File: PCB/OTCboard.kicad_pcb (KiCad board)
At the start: 4 copper layers, 0 parts

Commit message: cramming for portfolio
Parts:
- added C1: C, Capacitor_SMD:C_0603_1608Metric_Pad1.08x0.95mm_HandSolder, F.Cu at (90.7, 80.7)
- added C2: C, Capacitor_SMD:C_0603_1608Metric_Pad1.08x0.95mm_HandSolder, F.Cu at (90.7, 83.2)
- added C3: 0.1uF, Capacitor_SMD:C_0603_1608Metric_Pad1.08x0.95mm_HandSolder, F.Cu at (90.7, 85.7)
- added C4: 10u, Capacitor_SMD:C_0805_2012Metric_Pad1.18x1.45mm_HandSolder, F.Cu at (93.8, 68.9)
- added C5: 1u, Capacitor_SMD:C_0805_2012Metric_Pad1.18x1.45mm_HandSolder, F.Cu at (93.8, 71.9)
- added C6: 1u, Capacitor_SMD:C_0805_2012Metric_Pad1.18x1.45mm_HandSolder, F.Cu at (93.8, 74.9)
- added D1: 1N5819HW-7-F, Diode_SMD:D_SOD-123, F.Cu at (91.8, 64.3)
- added D2: SP0503BAHT, Package_TO_SOT_SMD:SOT-143, F.Cu at (95.4, 59.8)
- added D3: PWR, LED_SMD:LED_0603_1608Metric_Pad1.05x0.95mm_HandSolder, F.Cu at (91.1, 58.7)
- added D4: PWR, LED_SMD:LED_0603_1608Metric_Pad1.05x0.95mm_HandSolder, F.Cu at (91.1, 61.3)
- added D5: SK6812MINI, LED_SMD:LED_SK6812MINI_PLCC4_3.5x3.5mm_P1.75mm, F.Cu at (71.8, 60.0)
- added D6: SK6812MINI, LED_SMD:LED_SK6812MINI_PLCC4_3.5x3.5mm_P1.75mm, F.Cu at (71.8, 65.1)
- added D7: SK6812MINI, LED_SMD:LED_SK6812MINI_PLCC4_3.5x3.5mm_P1.75mm, F.Cu at (71.8, 70.2)
- added J1: USB_C_Receptacle_USB2.0_16P, Connector_USB:USB_C_Receptacle_GCT_USB4105-xx-A_16P_TopMnt_Horizontal, F.Cu at (132.1, 53.7)
- added J2: Display, Connector_PinHeader_2.54mm:PinHeader_1x08_P2.54mm_Vertical, F.Cu at (66.2, 59.7)
- added R1: 10k, Resistor_SMD:R_0603_1608Metric_Pad0.98x0.95mm_HandSolder, F.Cu at (90.7, 88.2)
- added R2: 5.1k, Resistor_SMD:R_0603_1608Metric_Pad0.98x0.95mm_HandSolder, F.Cu at (89.2, 68.6)
- added R3: 5.1k, Resistor_SMD:R_0603_1608Metric_Pad0.98x0.95mm_HandSolder, F.Cu at (89.2, 71.2)
- added R4: 450, Resistor_SMD:R_0603_1608Metric_Pad0.98x0.95mm_HandSolder, F.Cu at (89.2, 73.7)
- added R5: 120, Resistor_SMD:R_0603_1608Metric_Pad0.98x0.95mm_HandSolder, F.Cu at (89.2, 76.2)
- added U1: STM32G491CETx, Package_QFP:LQFP-48_7x7mm_P0.5mm, F.Cu at (82.9, 85.1)
- added U2: TLV1117-33, Package_TO_SOT_SMD:SOT-223, F.Cu at (82.1, 71.6)
- added U3: DRV5055A3xDBZxQ1, Package_TO_SOT_SMD:SOT-23, F.Cu at (66.4, 84.0)
- added U4: DRV5055A3xDBZxQ1, Package_TO_SOT_SMD:SOT-23, F.Cu at (66.4, 88.4)
- added U5: DRV5055A3xDBZxQ1, Package_TO_SOT_SMD:SOT-23, F.Cu at (66.4, 92.9)
- added Y1: Crystal, Crystal:Crystal_SMD_Abracon_ABM3-2Pin_5.0x3.2mm, F.Cu at (81.0, 93.4)

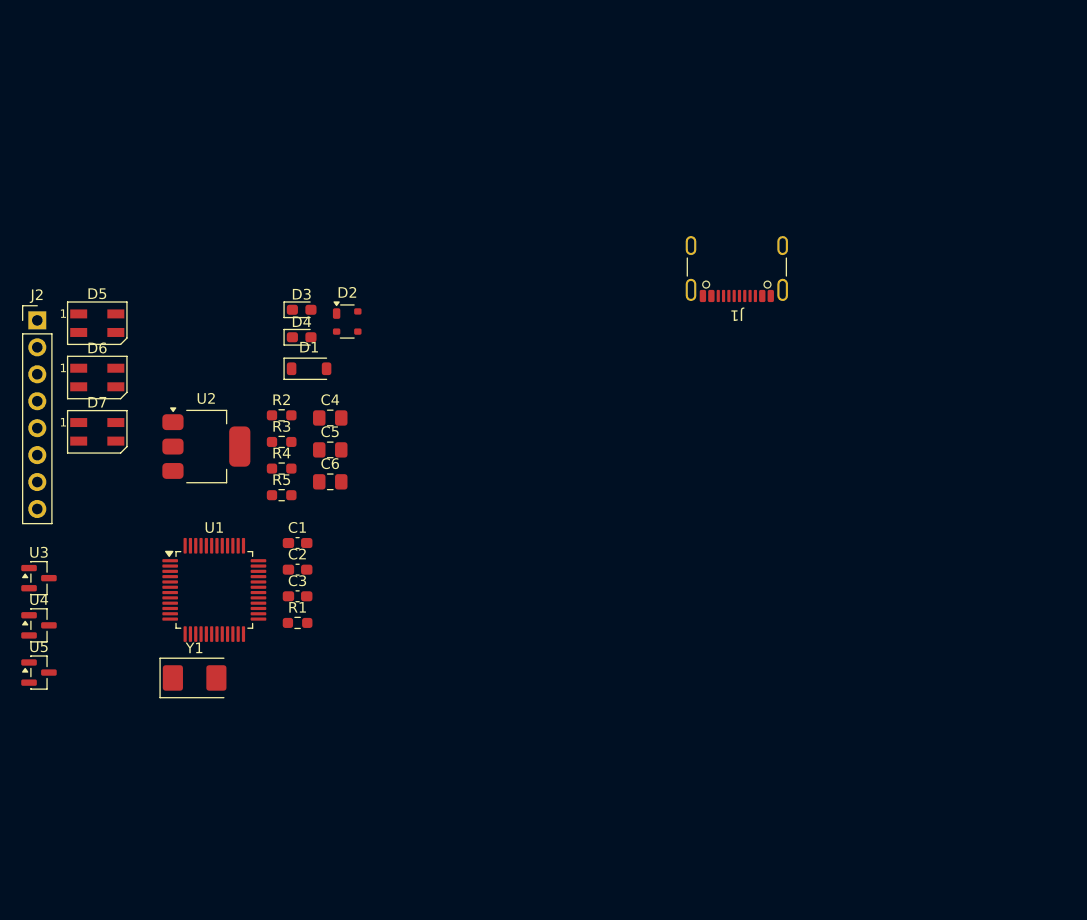
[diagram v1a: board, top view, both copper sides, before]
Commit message: only need to find boot and reset footprints
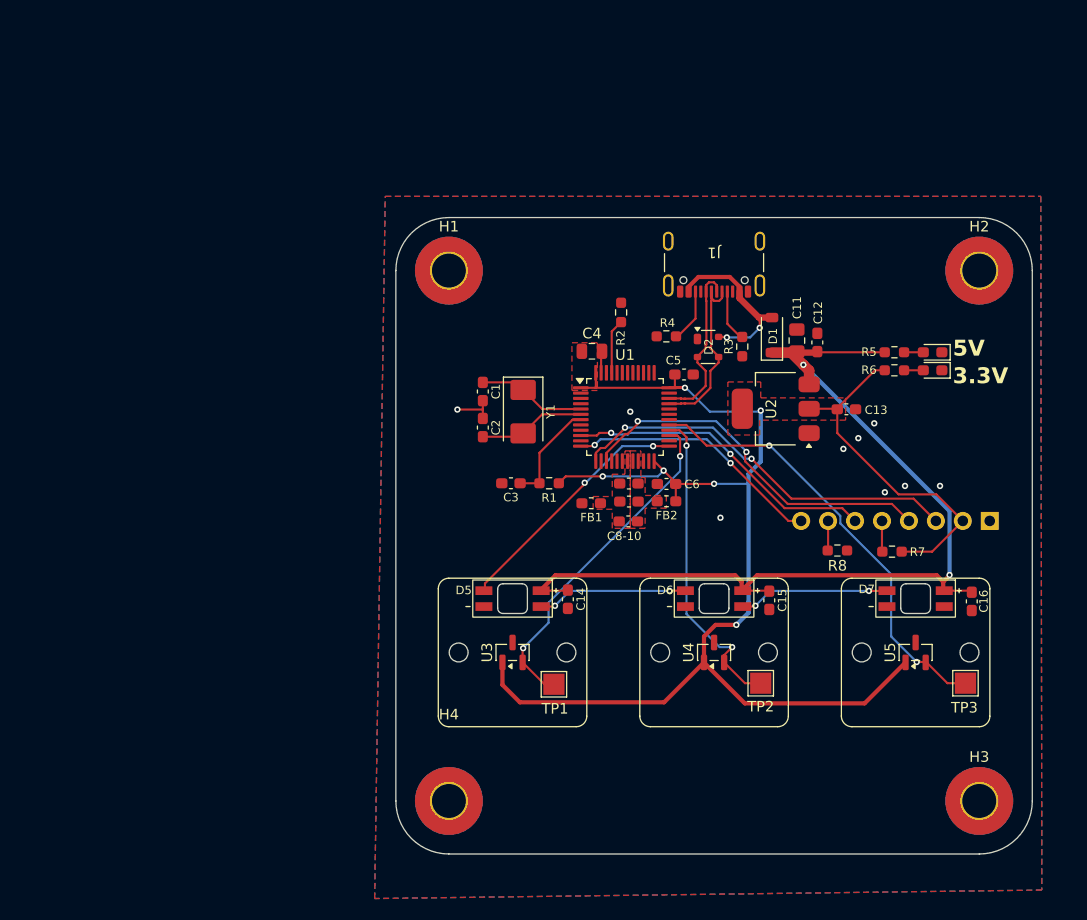
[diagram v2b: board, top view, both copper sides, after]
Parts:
- added C10: 0.1uF, Capacitor_SMD:C_0603_1608Metric_Pad1.08x0.95mm_HandSolder, F.Cu at (121.9, 78.6)
- added C11: 10u, Capacitor_SMD:C_0805_2012Metric_Pad1.18x1.45mm_HandSolder, F.Cu at (137.8, 61.6)
- added C12: 1u, Capacitor_SMD:C_0603_1608Metric_Pad1.08x0.95mm_HandSolder, F.Cu at (139.7, 61.8)
- added C13: 1u, Capacitor_SMD:C_0603_1608Metric_Pad1.08x0.95mm_HandSolder, F.Cu at (142.5, 68.1)
- added C14: 0.1u, Capacitor_SMD:C_0603_1608Metric_Pad1.08x0.95mm_HandSolder, F.Cu at (116.2, 86.0)
- added C15: 0.1u, Capacitor_SMD:C_0603_1608Metric_Pad1.08x0.95mm_HandSolder, F.Cu at (135.2, 86.1)
- added C16: 0.1u, Capacitor_SMD:C_0603_1608Metric_Pad1.08x0.95mm_HandSolder, F.Cu at (154.3, 86.2)
- added C8: 0.1uF, Capacitor_SMD:C_0603_1608Metric_Pad1.08x0.95mm_HandSolder, F.Cu at (122.0, 75.1)
- added C9: 0.1uF, Capacitor_SMD:C_0603_1608Metric_Pad1.08x0.95mm_HandSolder, F.Cu at (122.0, 76.8)
- added FB1: FerriteBead, Inductor_SMD:L_0603_1608Metric_Pad1.05x0.95mm_HandSolder, F.Cu at (118.4, 76.9)
- added FB2: FerriteBead, Inductor_SMD:L_0603_1608Metric_Pad1.05x0.95mm_HandSolder, F.Cu at (125.5, 76.8)
- added H1: MountingHole_Pad, MountingHole:MountingHole_3.2mm_M3_Pad_TopBottom, F.Cu at (105.0, 55.0)
- added H2: MountingHole_Pad, MountingHole:MountingHole_3.2mm_M3_Pad_TopBottom, F.Cu at (155.0, 55.0)
- added H3: MountingHole_Pad, MountingHole:MountingHole_3.2mm_M3_Pad_TopBottom, F.Cu at (155.0, 105.0)
- added H4: MountingHole_Pad, MountingHole:MountingHole_3.2mm_M3_Pad_TopBottom, F.Cu at (105.0, 105.0)
- added R6: 120, Resistor_SMD:R_0603_1608Metric_Pad0.98x0.95mm_HandSolder, F.Cu at (147.0, 64.4)
- added R7: 10k, Resistor_SMD:R_0603_1608Metric_Pad0.98x0.95mm_HandSolder, F.Cu at (146.8, 81.5)
- added R8: 10k, Resistor_SMD:R_0603_1608Metric_Pad0.98x0.95mm_HandSolder, F.Cu at (141.6, 81.4)
- added TP1: KEY1, TestPoint:TestPoint_Pad_2.0x2.0mm, F.Cu at (114.9, 94.0)
- added TP2: KEY2, TestPoint:TestPoint_Pad_2.0x2.0mm, F.Cu at (134.4, 93.9)
- added TP3: KEY3, TestPoint:TestPoint_Pad_2.0x2.0mm, F.Cu at (153.7, 93.9)
- added U6: ~, Magnetic Axis Switch:Cherry MX compatible, B.Cu at (111.0, 91.0)
- added U7: ~, Magnetic Axis Switch:Cherry MX compatible, B.Cu at (130.0, 91.0)
- added U8: ~, Magnetic Axis Switch:Cherry MX compatible, B.Cu at (149.0, 91.0)
- C3: value 0.1uF -> 0.1u
- C4: value 10u -> 4.7uF; footprint Capacitor_SMD:C_0805_2012Metric_Pad1.18x1.45mm_HandSolder -> Capacitor_SMD:C_0805_2012Metric
- C5, C6: value 1u -> 0.1uF; footprint Capacitor_SMD:C_0805_2012Metric_Pad1.18x1.45mm_HandSolder -> Capacitor_SMD:C_0603_1608Metric_Pad1.08x0.95mm_HandSolder
- D5, D6, D7: value SK6812MINI -> SK6812-E; footprint LED_SMD:LED_SK6812MINI_PLCC4_3.5x3.5mm_P1.75mm -> SK6812MINI-E:LED_SK6812-E
- J2: moved to B.Cu
- R2: value 5.1k -> 10k
- R4: value 450 -> 5.1k
- R5: value 120 -> 450
- moved J2 91.8 mm to (156.0, 78.6), turned to 90 degrees
- moved U5 82.7 mm to (149.0, 91.0), turned to 90 degrees
- moved D7 78.7 mm to (149.0, 85.9)
- moved U4 63.7 mm to (130.0, 91.0), turned to 90 degrees
- moved D6 61.8 mm to (130.0, 85.9)
- moved D3 59.6 mm to (150.6, 62.7), turned to 180 degrees
- moved D4 59.6 mm to (150.6, 64.4), turned to 180 degrees
- moved R5 59.3 mm to (147.0, 62.7)
- moved U2 53.8 mm to (135.8, 68.0), turned to 180 degrees
- moved D5 47.0 mm to (111.0, 85.9)
- moved U3 45.2 mm to (111.0, 91.0), turned to 90 degrees
- moved R3 44.3 mm to (132.7, 62.2), turned to -90 degrees
- moved D1 43.8 mm to (135.5, 61.1), turned to 90 degrees
- moved U1 42.0 mm to (121.6, 68.8)
- moved Y1 39.9 mm to (112.0, 68.3), turned to -90 degrees
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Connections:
- C4 pad 1: +5V -> +3.3V
- C5 pad 1: +5V -> +3.3V
- D2 pad 2: /USB/USB_D- -> /USB/USB_D+
- D2 pad 3: /USB/USB_D+ -> /USB/USB_D-
- D5 pad 1: Net-(D5-DOUT) -> +5V
- D5 pad 2: GND -> Net-(D5-DOUT)
- D5 pad 3: /LEDs/AddressableLEDs -> GND
- D5 pad 4: +5V -> /LEDs/AddressableLEDs
- D6 pad 1: Net-(D6-DOUT) -> +5V
- D6 pad 2: GND -> Net-(D6-DOUT)
- D6 pad 3: Net-(D5-DOUT) -> GND
- D6 pad 4: +5V -> Net-(D5-DOUT)
- D7 pad 1: unconnected-(D7-DOUT-Pad1) -> +5V
- D7 pad 2: GND -> unconnected-(D7-DOUT-Pad2)
- D7 pad 3: Net-(D6-DOUT) -> GND
- D7 pad 4: +5V -> Net-(D6-DOUT)
- J2 pad 5: /LEDs/RES -> Net-(J2-Pin_5)
- J2 pad 7: /LEDs/CS -> Net-(J2-Pin_7)
- R1 pad 2: +3V3 -> +3.3V
- R2 pad 1: /USB/CC1 -> /MCU/BOOT
- R2 pad 2: GND -> Net-(SW1-B)
- R3 pad 1: /USB/CC2 -> /USB/CC1
- R4 pad 1: +5V -> /USB/CC2
- R4 pad 2: Net-(D3-A) -> GND
- R5 pad 1: +3.3V -> +5V
- R5 pad 2: Net-(D4-A) -> Net-(D3-A)
- U1 pad 11: /LEDs/CS -> unconnected-(U1-PA3-Pad11)
- U1 pad 14: /MCU/MISO -> unconnected-(U1-PA6-Pad14)
- U1 pad 19: GND -> GNDA
- U1 pad 20: unconnected-(U1-VREF+-Pad20) -> +3V3A
- U1 pad 21: +3.3V -> +3V3A
- U1 pad 9: /LEDs/RES -> unconnected-(U1-PA1-Pad9)
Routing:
- net +3.3V: track 0.00 -> 149.3 mm, vias 0 -> 6
- net +5V: track 0.00 -> 93.6 mm, vias 0 -> 2
- net /Keys/KEY3: track 0.00 -> 41.9 mm, vias 0 -> 2
- net /LEDs/SCK: track 0.00 -> 37.5 mm, vias 0 -> 2
- net /LEDs/MOSI: track 0.00 -> 35.3 mm, vias 0 -> 2
- net /Keys/KEY1: track 0.00 -> 32.2 mm, vias 0 -> 2
- net /Keys/KEY2: track 0.00 -> 30.2 mm, vias 0 -> 2
- net /LEDs/DC: track 0.00 -> 29.5 mm, vias 0 -> 2
- net /LEDs/BL: track 0.00 -> 24.2 mm, vias 0 -> 2
- net /LEDs/AddressableLEDs: track 0.00 -> 23.5 mm, vias 0 -> 2
- net /USB/USB_D-: track 0.00 -> 16.8 mm
- net /USB/VBUSB: track 0.00 -> 16.2 mm, vias 0 -> 2
- net /USB/USB_D+: track 0.00 -> 16.1 mm
- net Net-(D5-DOUT): track 0.00 -> 14.4 mm, vias 0 -> 2
- net Net-(D6-DOUT): track 0.00 -> 14.4 mm, vias 0 -> 2
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- added copper zone on F.Cu, net +3.3V
- added copper zone on F.Cu, net +3V3A
- added copper zone on B.Cu, net GND
- added copper zone on F.Cu, net GND
- added copper zone on F.Cu, net GNDA
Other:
- board outline added: 60 x 60 mm
- copper layers 4 -> 2
- board text added: "3.3V"
- board text added: "5V"
- board text added: "C8-10"

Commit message: fixing this later
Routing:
- net /Keys/KEY2: track 30.2 -> 28.9 mm

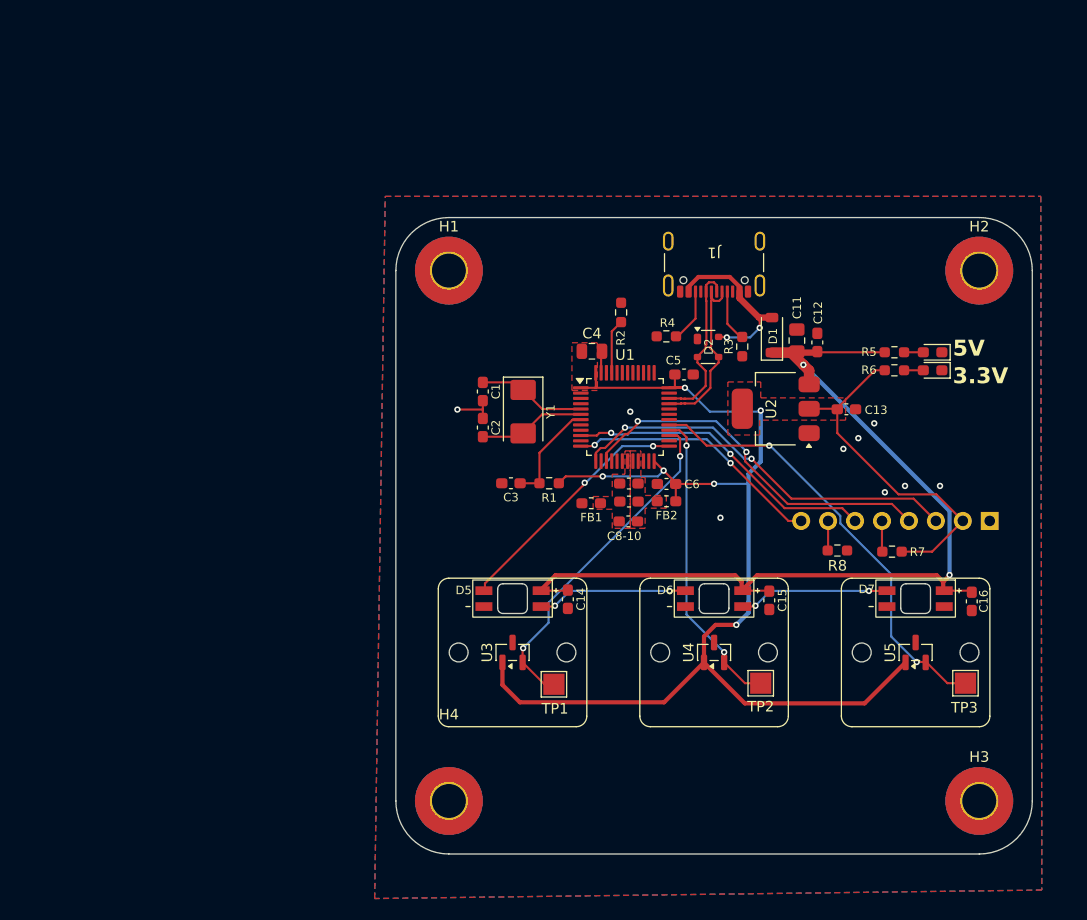
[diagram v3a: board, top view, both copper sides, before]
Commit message: changing to wasd
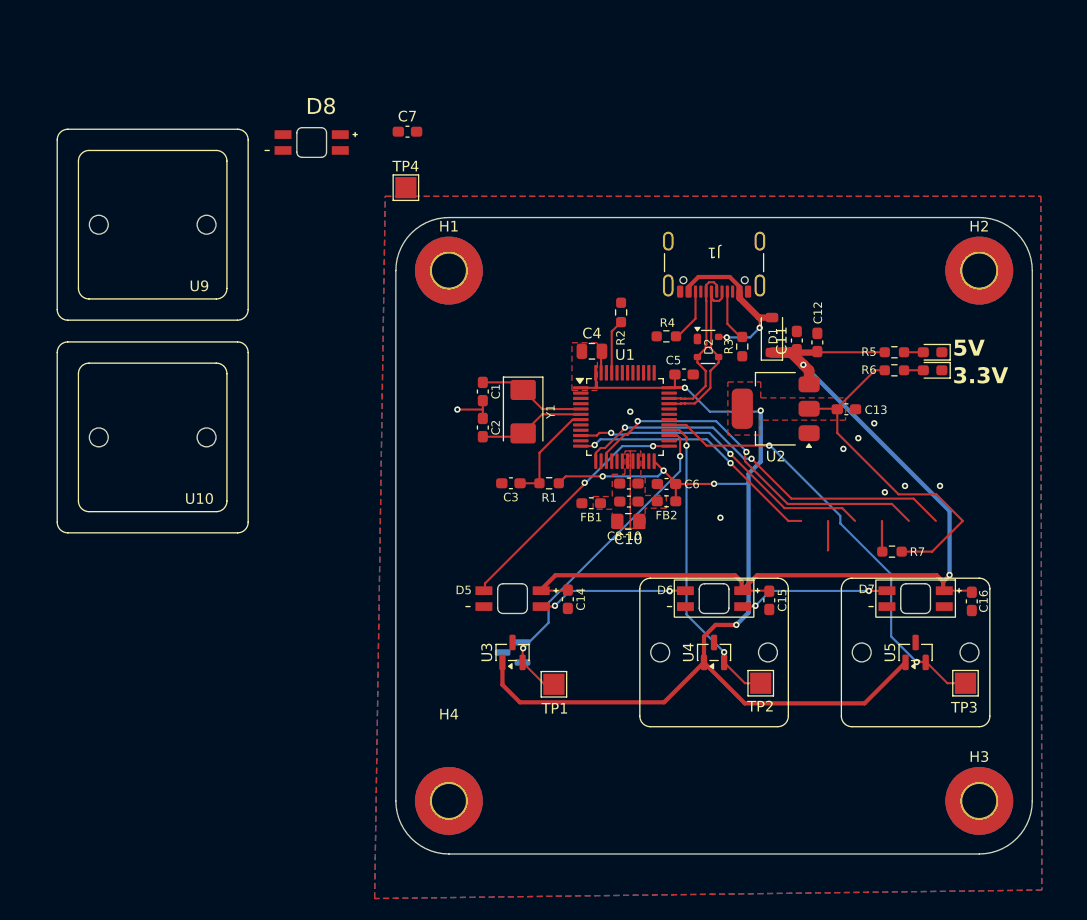
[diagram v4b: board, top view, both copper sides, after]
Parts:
- removed J2: Display, Connector_PinHeader_2.54mm:PinHeader_1x08_P2.54mm_Vertical
- removed R8: 10k, Resistor_SMD:R_0603_1608Metric_Pad0.98x0.95mm_HandSolder
- added C7: 0.1uF, Capacitor_SMD:C_0603_1608Metric_Pad1.08x0.95mm_HandSolder, F.Cu at (101.1, 41.9)
- added D8: SK6812-E, SK6812MINI-E:LED_SK6812-E, F.Cu at (92.1, 42.9)
- added TP4: KEY4, TestPoint:TestPoint_Pad_2.0x2.0mm, F.Cu at (100.9, 47.2)
- added U10: ~, Magnetic Axis Switch:Cherry MX compatible, F.Cu at (77.1, 70.7)
- added U9: ~, Magnetic Axis Switch:Cherry MX compatible, F.Cu at (77.1, 50.7)
- C10: value 0.1uF -> 10u; footprint Capacitor_SMD:C_0603_1608Metric_Pad1.08x0.95mm_HandSolder -> Capacitor_SMD:C_0805_2012Metric_Pad1.18x1.45mm_HandSolder
- C11: footprint Capacitor_SMD:C_0805_2012Metric_Pad1.18x1.45mm_HandSolder -> Capacitor_SMD:C_0603_1608Metric_Pad1.08x0.95mm_HandSolder
- C12: value 1u -> 10u
- C13: value 1u -> 0.1u
- R5: value 450 -> 1k
- R6: value 120 -> 1k
- U1: value STM32G491CETx -> STM32G431CBTx
- U2: value TLV1117-33 -> MCP1826S; footprint Package_TO_SOT_SMD:SOT-223 -> Package_TO_SOT_SMD:SOT-223-3_TabPin2
- U6: value ~ -> DRV5055A3xDBZxQ1; footprint Magnetic Axis Switch:Cherry MX compatible -> Package_TO_SOT_SMD:SOT-23
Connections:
- C10 pad 1: +3V3A -> +5V
- C10 pad 2: GNDA -> GND
- C12 pad 1: +5V -> +3.3V
- C13 pad 1: +3.3V -> +5V
- D7 pad 2: unconnected-(D7-DOUT-Pad2) -> Net-(D7-DOUT)
- R7 pad 1: +3.3V -> Net-(D8-DOUT)
- R7 pad 2: Net-(J2-Pin_5) -> GND
- U1 pad 10: /LEDs/DC -> unconnected-(U1-PA2-Pad10)
- U1 pad 12: /LEDs/BL -> unconnected-(U1-PA4-Pad12)
- U1 pad 13: /LEDs/SCK -> unconnected-(U1-PA5-Pad13)
- U1 pad 15: /LEDs/MOSI -> unconnected-(U1-PA7-Pad15)
- U1 pad 26: unconnected-(U1-PB12-Pad26) -> /Keys/KEY1
- U1 pad 27: /Keys/KEY1 -> /Keys/KEY2
- U1 pad 28: /Keys/KEY2 -> /Keys/KEY3
- U1 pad 29: /Keys/KEY3 -> /Keys/KEY4
- U2 pad 1: GND -> +5V
- U2 pad 2: +3.3V -> GND
- U2 pad 3: +5V -> +3.3V
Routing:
- net unconnected-(U1-PA5-Pad13): track 0.00 -> 37.5 mm, vias 0 -> 2
- net /LEDs/SCK: track 37.5 -> 0.00 mm, vias 2 -> 0
- net unconnected-(U1-PA7-Pad15): track 0.00 -> 35.3 mm, vias 0 -> 2
- net /LEDs/MOSI: track 35.3 -> 0.00 mm, vias 2 -> 0
- net unconnected-(U1-PA2-Pad10): track 0.00 -> 29.5 mm, vias 0 -> 2
- net /LEDs/DC: track 29.5 -> 0.00 mm, vias 2 -> 0
- net unconnected-(U1-PA4-Pad12): track 0.00 -> 24.2 mm, vias 0 -> 2
- net /LEDs/BL: track 24.2 -> 0.00 mm, vias 2 -> 0
- net Net-(J2-Pin_5): track 2.91 -> 0.00 mm
- net GND: track 6.14 -> 9.05 mm
- net Net-(J2-Pin_7): track 2.81 -> 0.00 mm
- net (no net): track 0.00 -> 2.81 mm

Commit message: new update
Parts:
- added C17: 0.1u, Capacitor_SMD:C_0603_1608Metric_Pad1.08x0.95mm_HandSolder, F.Cu at (118.1, 34.0)
- added C18: 0.1u, Capacitor_SMD:C_0603_1608Metric_Pad1.08x0.95mm_HandSolder, F.Cu at (118.1, 36.5)
- added C19: 0.1u, Capacitor_SMD:C_0603_1608Metric_Pad1.08x0.95mm_HandSolder, F.Cu at (118.1, 39.0)
- added C20: 0.1u, Capacitor_SMD:C_0603_1608Metric_Pad1.08x0.95mm_HandSolder, F.Cu at (118.1, 41.5)
- added TP5: KEY3, TestPoint:TestPoint_Loop_D2.54mm_Drill1.5mm_Beaded, F.Cu at (124.3, 34.7)
- added TP6: KEY4, TestPoint:TestPoint_Loop_D2.54mm_Drill1.5mm_Beaded, F.Cu at (125.3, 41.3)
- C1, C2: value C -> 26p
- C11, C12: footprint Capacitor_SMD:C_0603_1608Metric_Pad1.08x0.95mm_HandSolder -> Capacitor_SMD:C_0805_2012Metric_Pad1.18x1.45mm_HandSolder
- C4: footprint Capacitor_SMD:C_0805_2012Metric -> Capacitor_SMD:C_0805_2012Metric_Pad1.18x1.45mm_HandSolder
- R3, R4, U9: moved to B.Cu
- TP1: value KEY1 -> TestPoint; footprint TestPoint:TestPoint_Pad_2.0x2.0mm -> TestPoint:TestPoint_Loop_D2.54mm_Drill1.5mm_Beaded
- TP2: value KEY2 -> TestPoint; footprint TestPoint:TestPoint_Pad_2.0x2.0mm -> TestPoint:TestPoint_Loop_D2.54mm_Drill1.5mm_Beaded
- TP3: value KEY3 -> KEY1; footprint TestPoint:TestPoint_Pad_2.0x2.0mm -> TestPoint:TestPoint_Loop_D2.54mm_Drill1.5mm_Beaded
- TP4: value KEY4 -> KEY2; footprint TestPoint:TestPoint_Pad_2.0x2.0mm -> TestPoint:TestPoint_Loop_D2.54mm_Drill1.5mm_Beaded
- U6, U8: moved to F.Cu
- moved U9 86.1 mm to (149.0, 98.0), turned to 180 degrees
- moved U10 53.6 mm to (130.0, 79.0)
- moved TP1 49.4 mm to (147.5, 57.0)
- moved C13 47.9 mm to (96.1, 79.8)
- moved TP3 47.2 mm to (107.2, 102.2)
- moved TP2 30.7 mm to (147.8, 66.3)
- moved H3 27.4 mm to (155.0, 77.6)
- moved H4 24.4 mm to (103.8, 80.7)
- moved U7 20.2 mm to (111.0, 98.0)
- moved U8 20.2 mm to (130.0, 98.0), turned to 0 degrees
- moved C15 18.6 mm to (146.6, 100.7)
- moved U6 17.6 mm to (93.7, 94.2), turned to 90 degrees
- moved C12 11.4 mm to (135.4, 72.3), turned to 0 degrees
- moved D5 7.00 mm to (111.0, 92.9)
- moved D6 7.00 mm to (130.0, 92.9)
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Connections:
- C13 pad 1: +5V -> +3.3V
- C14 pad 1: +5V -> +3.3V
- C15 pad 1: +5V -> +3.3V
- C16 pad 1: +5V -> +3.3V
- TP1 pad 1: /Keys/KEY1 -> +5V
- TP2 pad 1: /Keys/KEY2 -> +3.3V
- TP3 pad 1: /Keys/KEY3 -> /Keys/KEY1
- TP4 pad 1: /Keys/KEY4 -> /Keys/KEY2
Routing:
- net +3.3V: track 149.3 -> 0.00 mm, vias 6 -> 0
- net +5V: track 93.6 -> 0.00 mm, vias 2 -> 0
- net /Keys/KEY3: track 41.9 -> 0.00 mm, vias 2 -> 0
- net unconnected-(U1-PA5-Pad13): track 37.5 -> 0.00 mm, vias 2 -> 0
- net unconnected-(U1-PA7-Pad15): track 35.3 -> 0.00 mm, vias 2 -> 0
- net /Keys/KEY1: track 32.2 -> 0.00 mm, vias 2 -> 0
- net unconnected-(U1-PA2-Pad10): track 29.5 -> 0.00 mm, vias 2 -> 0
- net /Keys/KEY2: track 28.9 -> 0.00 mm, vias 2 -> 0
- net unconnected-(U1-PA4-Pad12): track 24.2 -> 0.00 mm, vias 2 -> 0
- net /LEDs/AddressableLEDs: track 23.5 -> 0.00 mm, vias 2 -> 0
- net /USB/USB_D-: track 16.8 -> 0.00 mm
- net /USB/VBUSB: track 16.2 -> 0.00 mm, vias 2 -> 0
- net /USB/USB_D+: track 16.1 -> 0.00 mm
- net Net-(D5-DOUT): track 14.4 -> 0.00 mm, vias 2 -> 0
- net Net-(D6-DOUT): track 14.4 -> 0.00 mm, vias 2 -> 0
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- removed copper zone on F.Cu, net +3.3V
